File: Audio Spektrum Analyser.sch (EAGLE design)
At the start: 132 parts, among them IC1 LM324N, IC10 LM3914N, IC11 LM3914N, IC12 LM3914N, IC13 LM3914N, IC2 LM324N, IC3 LM324N, IC4 LM3914N, IC5 LM3914N, IC6 LM3914N, IC7 LM3914N, IC8 LM3914N, IC9 LM3914N, M1 ELECTRET_MICROPHON-F6050AP

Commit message: connected bandpass
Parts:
- removed R63: 10k, resistor:R-TRIMM3339P
- added C33, C34, C35: 1u, resistor:CPOL-EUE2.5-5
- added C36, C37, C38, C39, C40, C41, C42, C43, C44, C45: 100n, resistor:C-EU050-024X044
- added R4: 47k, rcl:R-EU_0207/7
- C10: value 1n2 -> 1u; device resistor:C-EU025-024X044 -> resistor:CPOL-EUE2.5-5
- C11: value 620p -> 1u; device resistor:C-EU025-024X044 -> resistor:CPOL-EUE2.5-5
- C16: value 1u -> 4n7; device resistor:CPOL-EUE2.5-5 -> resistor:C-EU025-024X044
- C17: value 1u -> 2n2; device resistor:CPOL-EUE2.5-5 -> resistor:C-EU025-024X044
- C18: value 1u -> 1n2; device resistor:CPOL-EUE2.5-5 -> resistor:C-EU025-024X044
- C19: value 1u -> 620p; device resistor:CPOL-EUE2.5-5 -> resistor:C-EU025-024X044
- C2, C4: value 22n -> 100n; device resistor:C-EU025-024X044 -> resistor:C-EU050-024X044
- C20: value 330p -> 1u; device resistor:C-EU025-024X044 -> resistor:CPOL-EUE2.5-5
- C21: value 160p -> 1u; device resistor:C-EU025-024X044 -> resistor:CPOL-EUE2.5-5
- C22: value 82p -> 1u; device resistor:C-EU025-024X044 -> resistor:CPOL-EUE2.5-5
- C23: value 39p -> 1u; device resistor:C-EU025-024X044 -> resistor:CPOL-EUE2.5-5
- C28: value 1u -> 330p; device resistor:CPOL-EUE2.5-5 -> resistor:C-EU025-024X044
- C29: value 1u -> 160p; device resistor:CPOL-EUE2.5-5 -> resistor:C-EU025-024X044
- C3: value 10n -> 100u; device resistor:C-EU025-024X044 -> resistor:CPOL-EUE5-10.5
- C30: value 1u -> 82p; device resistor:CPOL-EUE2.5-5 -> resistor:C-EU025-024X044
- C31: value 1u -> 39p; device resistor:CPOL-EUE2.5-5 -> resistor:C-EU025-024X044
- C32: value 100u -> 1u; device resistor:CPOL-EUE5-10.5 -> resistor:CPOL-EUE2.5-5
- C5: value 10n -> 100n; device resistor:C-EU025-024X044 -> resistor:C-EU050-024X044
- C6: value 1u -> 22n; device resistor:CPOL-EUE2.5-5 -> resistor:C-EU025-024X044
- C7: value 1u -> 10n; device resistor:CPOL-EUE2.5-5 -> resistor:C-EU025-024X044
- C8: value 4n7 -> 22n
- C9: value 2n2 -> 10n
- J1: device Jakobs_LBR:2.5MM-AUX -> Jakobs_LBR:2.5MM-AUXPC
- R1: value 10k -> 4k7; device rcl:R-EU_0207/7 -> resistor:R-TRIMM3339P
- R10, R11: value 1k2 -> 10k; device resistor:R-EU_0207/7 -> resistor:R-TRIMM3339P
- R12, R13, R19, R20, R21, R22, R23, R24, R31, R32, R33, R34, R35, R36: value 1k2 -> 120k
- R14, R15, R25, R26, R37, R38: value 1M -> 120k
- R17, R18, R29, R30, R41: value 1k2 -> 1M
- R3: value 4k7 -> 10k; device resistor:R-TRIMM3339P -> rcl:R-EU_0207/7
- R42: value 7k5 -> 1M
- R5: value 10k -> 47k
- R61: value 10k -> 1k2; device resistor:R-TRIMM3339P -> resistor:R-EU_0207/7
- R62: value 10k -> 7k5; device rcl:R-EU_0207/7 -> resistor:R-EU_0207/7
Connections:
- net +5V: now also C2.1, C36.1, C37.1, C38.1, C39.1, C4.1, C40.1, C41.1, C42.1, C43.1, C44.1, C45.1, C5.1, R1.E, R16.2, R4.2; no longer R14.2, R3.E, R62.2
- net GND: now also C10.-, C11.-, C2.2, C20.-, C21.-, C22.-, C23.-, C32.-, C33.-, C34.-, C35.-, C36.2, C37.2, C38.2, C39.2, C4.2, C40.2, C41.2, C42.2, C43.2, C44.2, C45.2, C5.2, R14.1, R15.1, R25.1, R26.1, R37.1, R38.1, R62.1; no longer C16.-, C17.-, C18.-, C19.-, C28.-, C29.-, C30.-, C31.-, C6.-, C7.-, R12.1, R13.1, R21.1, R22.1, R33.1, R34.1, R42.1
- net N$1: now also R2.1; no longer R1.1
- net N$10: now also R11.E; no longer R63.E
- net N$107: now also R43.2; no longer R41.2
- net N$108: now also R43.1, R44.2; no longer R41.1, R42.2
- net N$12: now also C3.+; no longer C1.+
- net N$120: now also R57.2; no longer R55.2
- net N$121: now also R57.1, R58.2; no longer R55.1, R56.2
- net N$125: now also C16.2, R27.2; no longer C12.2, R25.2
- net N$127: now also R59.2; no longer R57.2
- net N$128: now also R59.1, R60.2; no longer R57.1, R58.2
- net N$13: now also C1.+, R1.A; no longer C32.+, R3.A
- net N$130: now also C12.2, R27.1; no longer C8.2, R25.1
- net N$133: now also C8.2, R17.2; no longer C4.2, R15.2
- net N$134: now also C6.2, R17.1; no longer C2.2, R15.1
- net N$135: now also C19.2, R30.2; no longer C15.2, R28.2
- net N$136: now also C6.1, C8.1, R14.2; no longer C2.1, C4.1, R10.2
- net N$138: now also C9.2, R18.2; no longer C5.2, R16.2
- net N$139: now also C7.2, R18.1; no longer C3.2, R16.1
- net N$140: now also C16.1, R19.2, R23.2; no longer C8.1, R17.2, R21.2
- net N$141: now also C7.1, C9.1, R15.2; no longer C3.1, C5.1, R11.2
- net N$144: now also C17.2, R28.2; no longer C13.2, R26.2
- net N$145: now also C13.2, R28.1; no longer C9.2, R26.1
- net N$146: now also C15.2, R30.1; no longer C11.2, R28.1
- net N$147: now also C17.1, R20.2, R24.2; no longer C9.1, R18.2, R22.2
- net N$149: now also C18.2, R29.2; no longer C14.2, R27.2
- net N$150: now also C14.2, R29.1; no longer C10.2, R27.1
- net N$151: now also C28.2, R39.2; no longer C24.2, R37.2
- net N$152: now also C18.1, R21.2, R25.2; no longer C10.1, R19.2, R23.2
- net N$154: now also C19.1, R22.2, R26.2; no longer C11.1, R20.2, R24.2
- net N$156: now also C24.2, R39.1; no longer C20.2, R37.1
- net N$157: now also C28.1, R31.2, R35.2; no longer C20.1, R29.2, R33.2
- net N$159: now also C29.2, R40.2; no longer C25.2, R38.2
- net N$160: now also C25.2, R40.1; no longer C21.2, R38.1
- net N$161: now also C29.1, R32.2, R36.2; no longer C21.1, R30.2, R34.2
- net N$163: now also C30.2, R41.2; no longer C26.2, R39.2
- net N$164: now also C26.2, R41.1; no longer C22.2, R39.1
- net N$165: now also C30.1, R33.2, R37.2; no longer C22.1, R31.2, R35.2
- net N$167: now also C31.2, R42.2; no longer C27.2, R40.2
- net N$168: now also C27.2, R42.1; no longer C23.2, R40.1
- net N$169: now also C31.1, R34.2, R38.2; no longer C23.1, R32.2, R36.2
- net N$179: now also R61.2; no longer R59.2
- net N$180: now also R61.1, R62.2; no longer R59.1, R60.2
- net N$2: now also R3.1; no longer R2.1
- net N$29: now also R47.2; no longer R45.2
- net N$3: now also R3.2; no longer R1.2
- net N$30: now also R47.1, R48.2; no longer R45.1, R46.2
- net N$31: now also R10.A; no longer R61.A
- net N$4: now also C1.-, R4.1; no longer C32.-, R62.1
- net N$42: now also R45.2; no longer R43.2
- net N$43: now also R45.1, R46.2; no longer R43.1, R44.2
- net N$44: now also R11.A; no longer R63.A
- net N$55: now also R49.2; no longer R47.2
- net N$56: now also R49.1, R50.2; no longer R47.1, R48.2
- net N$6: now also R10.E; no longer R61.E
- net N$68: now also R51.2; no longer R49.2
- net N$69: now also R51.1, R52.2; no longer R49.1, R50.2
- net N$81: now also R55.2; no longer R53.2
- net N$82: now also R55.1, R56.2; no longer R53.1, R54.2
- net N$94: now also R53.2; no longer R51.2
- net N$95: now also R53.1, R54.2; no longer R51.1, R52.2
- net OUT1: now also C10.+; no longer C6.+
- net OUT10: now also C35.+; no longer C31.+
- net OUT2: now also C11.+; no longer C7.+
- net OUT3: now also C20.+; no longer C16.+
- net OUT4: now also C21.+; no longer C17.+
- net OUT5: now also C22.+; no longer C18.+
- net OUT6: now also C23.+; no longer C19.+
- net OUT7: now also C32.+; no longer C28.+
- net OUT8: now also C33.+; no longer C29.+
- net OUT9: now also C34.+; no longer C30.+
- net REF: now also R16.1; no longer R14.1
- net VER: now also C3.-, R12.1, R13.1, R21.1, R22.1, R33.1, R34.1; no longer C1.-, R10.1, R11.1, R17.1, R18.1, R29.1, R30.1
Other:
- moved on the sheet: C1, C12, C13, C14, C15, C2, C24, C25, C26, C27, C4, C5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

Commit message: created final shape
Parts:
- R16: value 1M -> 22k
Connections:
- removed net N$124: IC1B.+IN
- net N$3: now also IC1B.+IN

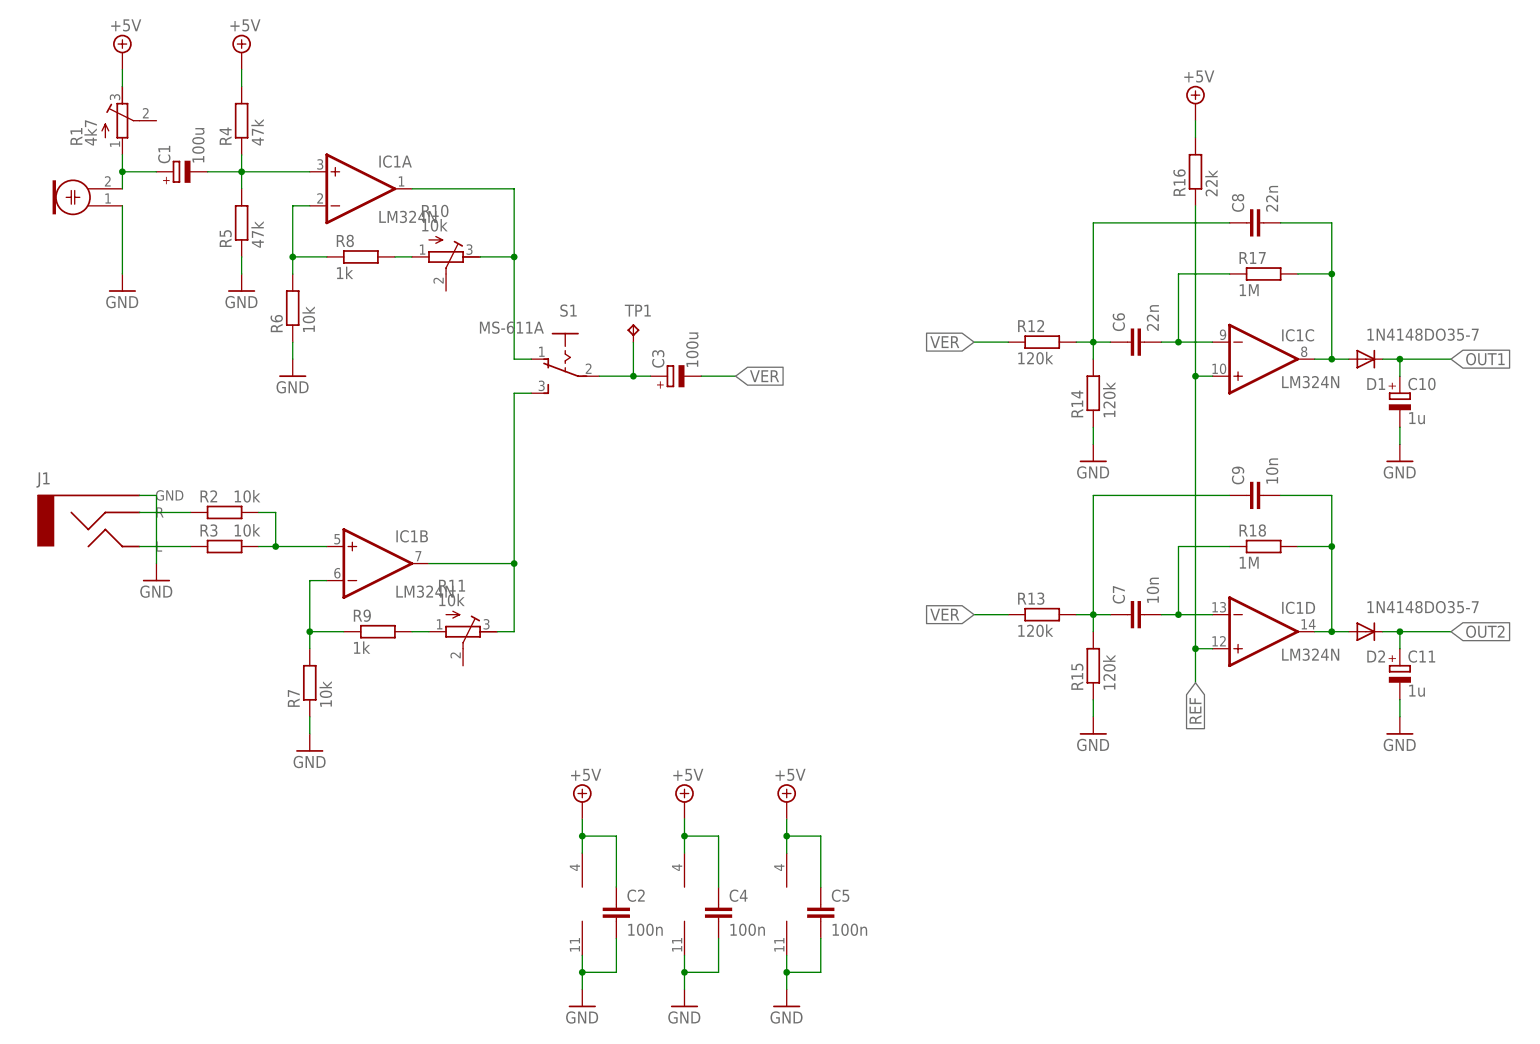
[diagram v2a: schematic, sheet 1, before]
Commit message: replaced dc blocking caps, print back side, added dc jack
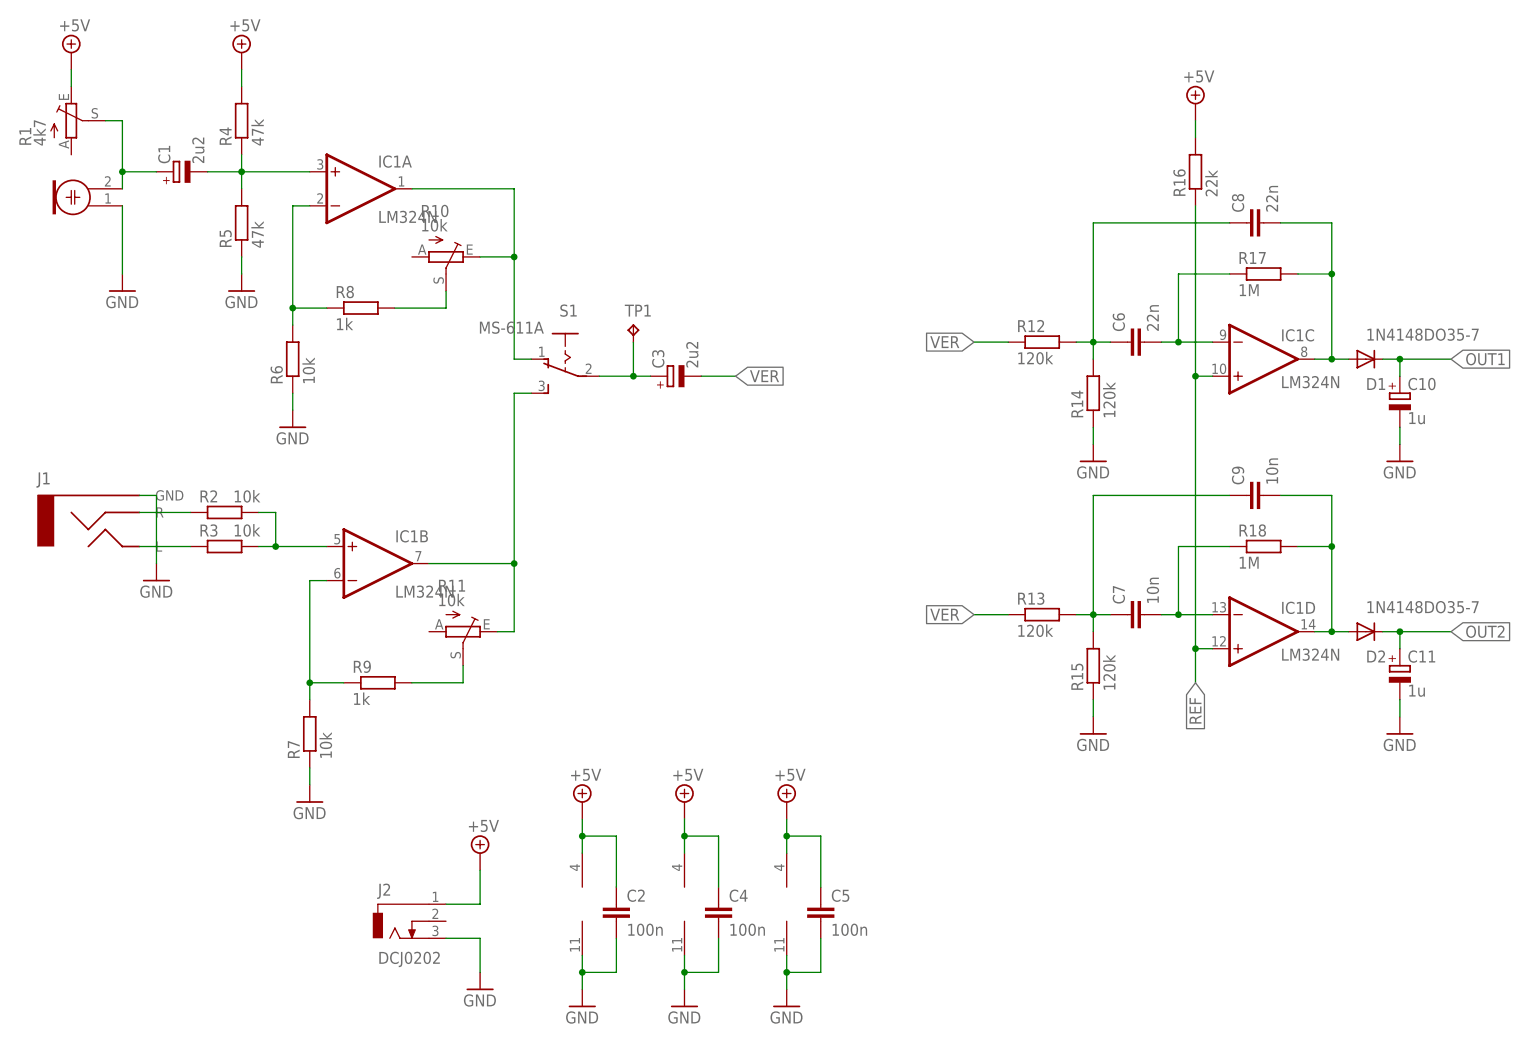
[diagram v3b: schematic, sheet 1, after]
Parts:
- added J2: DCJ0202, con-jack:DCJ0202
- C1, C3: value 100u -> 2u2; device resistor:CPOL-EUE5-10.5 -> resistor:CPOL-EUE2.5-5
- R1, R10, R11: device resistor:R-TRIMM3339P -> pot:TRIM_EU-CA6V
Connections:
- net +5V: now also J2.1
- net GND: now also J2.3
- net N$13: now also R1.S; no longer R1.A
- net N$31: now also R10.S; no longer R10.A
- net N$44: now also R11.S; no longer R11.A
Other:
- moved on the sheet: R6, R7, R8, R9

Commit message: updated to eagle 9.1.1
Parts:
- added TP2, TP3: TPPAD1-20, testpad:TPPAD1-20
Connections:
- net +5V: now also TP3.TP
- net GND: now also TP2.TP
- net N$12: no longer TP1.TP
- net VER: now also TP1.TP
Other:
- moved on the sheet: C3, J2, TP1
